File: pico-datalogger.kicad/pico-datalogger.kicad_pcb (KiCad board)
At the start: 2 copper layers, 80 x 90 mm, 28 parts, among them J1 JST-PH2 VCC, J10 Conn_Inky_SW, J2 Conn_I2C_Internal, J3 RFM9x_Lora_Breakout, J4 Alt-VCC, J5 Conn_I2S, J6 Conn_Inky_SPI, J7 Micro_SD_TF_PUSH, J8 Conn_ADC, J9 Conn_UART, SW1 SW_Push_SLIM, SW2 SW_Reset, U1 SN74HC74N, U2 PCF8523T, U3 Pico, Y1 Crystal

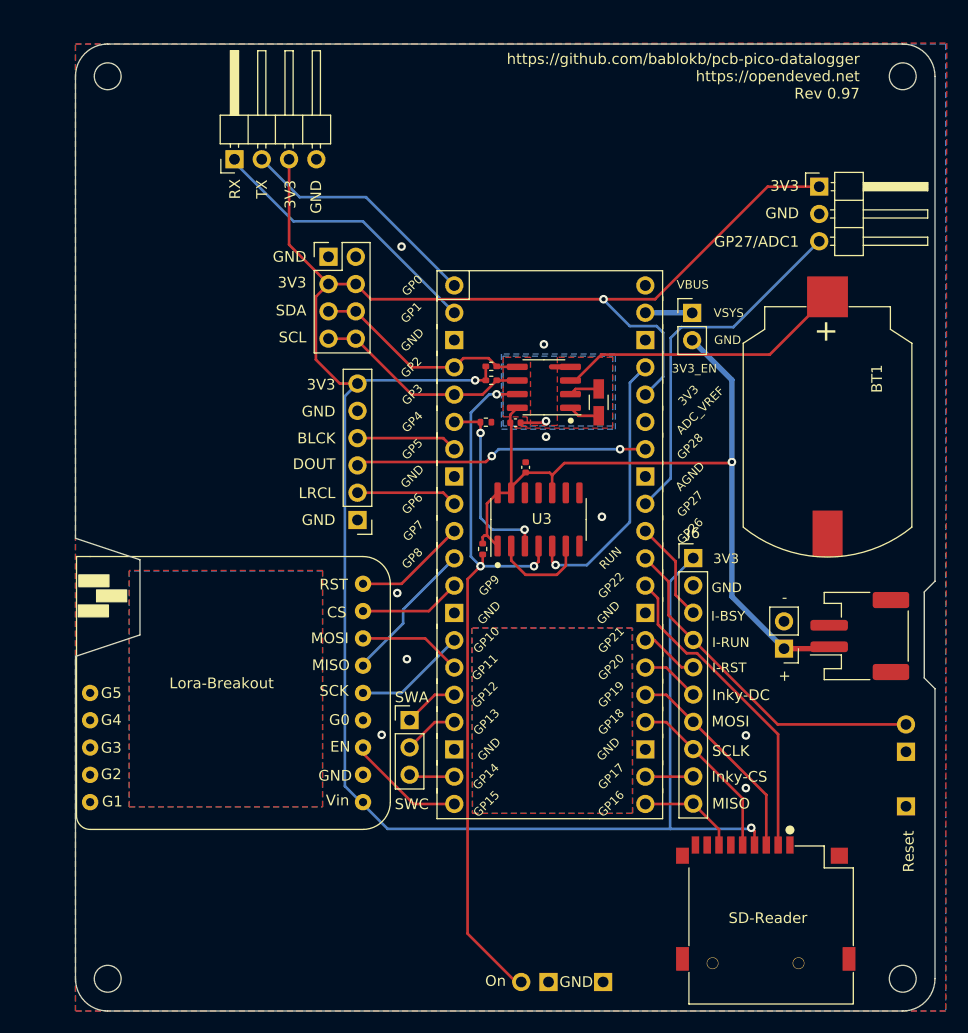
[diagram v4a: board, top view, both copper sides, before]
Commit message: added I2C/BG connectors
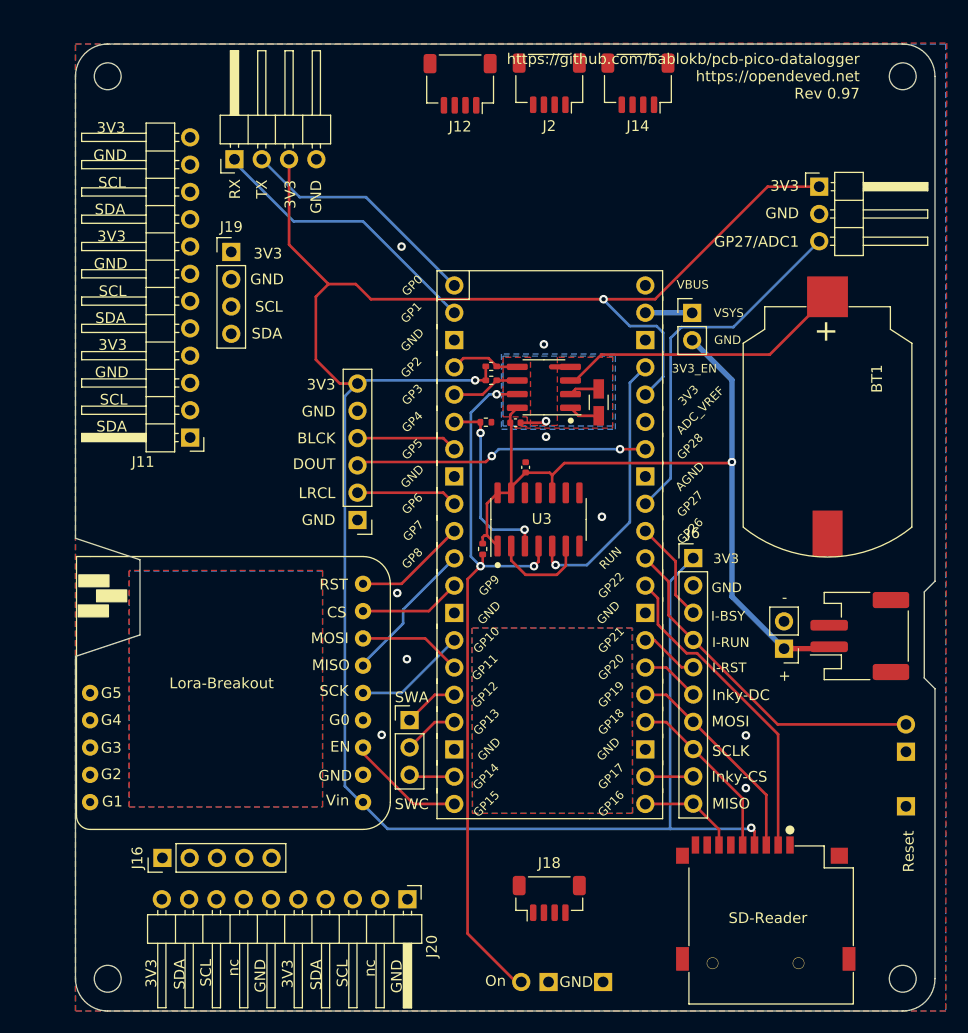
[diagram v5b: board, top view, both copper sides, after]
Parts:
- added J11: I2C_1, Connector_PinHeader_2.54mm:PinHeader_1x12_P2.54mm_Horizontal, F.Cu at (110.7, 86.6)
- added J12: I2C_7, Connector_JST:JST_SH_SM04B-SRSS-TB_1x04-1MP_P1.00mm_Horizontal, F.Cu at (135.8, 53.7)
- added J14: I2C_6, Connector_JST:JST_SH_SM04B-SRSS-TB_1x04-1MP_P1.00mm_Horizontal, F.Cu at (152.3, 53.6)
- added J16: BG_2, Connector_PinHeader_2.54mm:PinHeader_1x05_P2.54mm_Vertical, F.Cu at (108.1, 125.8)
- added J18: I2C_5, Connector_JST:JST_SH_BM04B-SRSS-TB_1x04-1MP_P1.00mm_Vertical, F.Cu at (144.1, 129.5)
- added J19: I2C_4, Connector_PinHeader_2.54mm:PinHeader_1x04_P2.54mm_Vertical, F.Cu at (114.5, 69.3)
- added J20: BG_3, Connector_PinHeader_2.54mm:PinHeader_1x10_P2.54mm_Horizontal, F.Cu at (130.9, 129.6)
- J2: value Conn_I2C_Internal -> I2C_8; footprint Connector_PinHeader_2.54mm:PinHeader_2x04_P2.54mm_Vertical -> Connector_JST:JST_SH_SM04B-SRSS-TB_1x04-1MP_P1.00mm_Horizontal
- moved J2 26.1 mm to (144.1, 53.6), turned to 180 degrees
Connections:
- J2 pad 1: GND -> +3V3
- J2 pad 3: +3V3 -> /SCL
- J2 pad 4: +3V3 -> /SDA
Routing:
- net /SDA: track 20.4 -> 6.55 mm
- net /SCL: track 20.3 -> 6.42 mm
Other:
- board text added: "nc"

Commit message: Rev 0.98: ready for production
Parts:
- added G***: LOGO, LOGO, B.Cu at (144.3, 66.4)
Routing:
- net /SCL: track 6.42 -> 204.3 mm, vias 0 -> 1
- net /SDA: track 6.55 -> 202.3 mm, vias 0 -> 2
- net +3V3: track 208.0 -> 299.9 mm, vias 3 -> 6
- net GND: vias 10 -> 13
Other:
- board text added: "BATT"
- board text added: "CR2032"
- board text added: "I2C"
- board text added: "I2C QT/Qwiic"
- board text added: "I2S"
- board text added: "MISO1"
- board text added: "MOSI1"
- board text added: "SCLK1"
- board text added: "UART"
- board text added: "https://github.com/bablokb/pcb-pico-datalogger https://opendeved.net/ilce Rev 0.98"
- board text removed: "MISO"
- board text removed: "MOSI"
- board text removed: "SCLK"
- board text removed: "https://github.com/bablokb/pcb-pico-datalogger https://opendeved.net Rev 0.97"

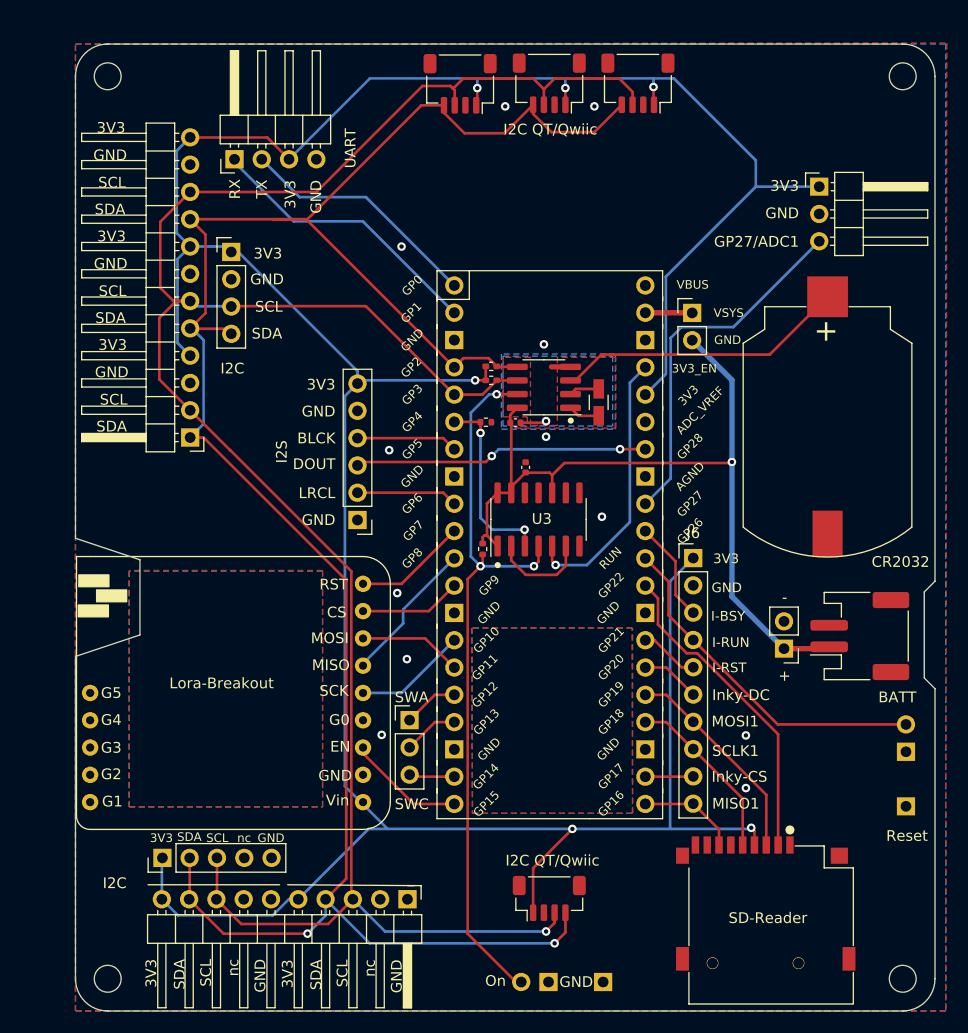
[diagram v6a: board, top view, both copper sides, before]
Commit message: Rev 1.00: fix Stemma/Qt connectors
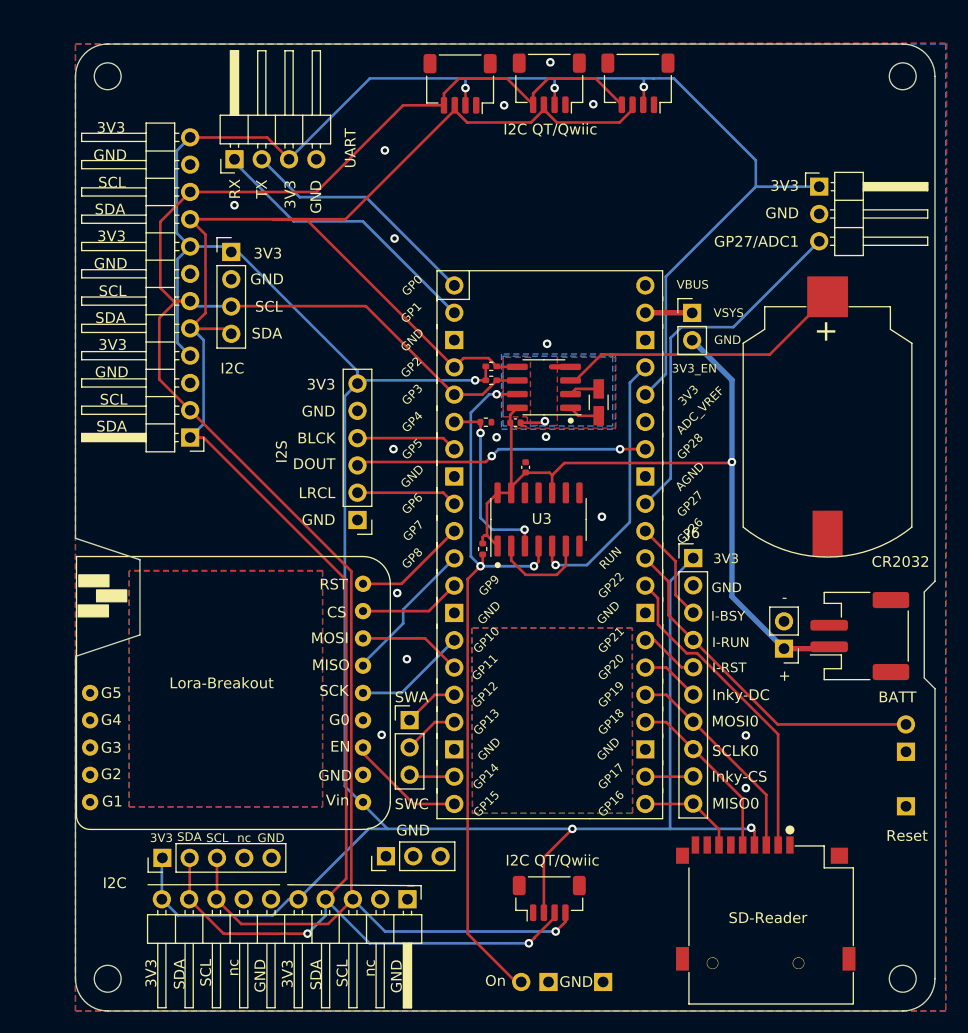
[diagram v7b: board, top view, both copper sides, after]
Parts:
- added J21: Conn_GND, Connector_PinHeader_2.54mm:PinHeader_1x03_P2.54mm_Vertical, F.Cu at (128.9, 125.6)
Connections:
- J12 pad 1: +3V3 -> GND
- J12 pad 2: GND -> +3V3
- J12 pad 3: /SCL -> /SDA
- J12 pad 4: /SDA -> /SCL
- J14 pad 1: +3V3 -> GND
- J14 pad 2: GND -> +3V3
- J14 pad 3: /SCL -> /SDA
- J14 pad 4: /SDA -> /SCL
- J18 pad 1: +3V3 -> GND
- J18 pad 2: GND -> +3V3
- J18 pad 3: /SCL -> /SDA
- J18 pad 4: /SDA -> /SCL
- J2 pad 1: +3V3 -> GND
- J2 pad 2: GND -> +3V3
- J2 pad 3: /SCL -> /SDA
- J2 pad 4: /SDA -> /SCL
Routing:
- net /SDA: track 202.3 -> 199.4 mm
- net /SCL: track 204.3 -> 202.7 mm
- net +3V3: track 299.9 -> 299.2 mm
- net GND: track 4.27 -> 4.17 mm, vias 13 -> 17
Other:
- board text added: "MISO0"
- board text added: "MOSI0"
- board text added: "SCLK0"
- board text added: "https://github.com/bablokb/pcb-pico-datalogger https://opendeved.net/ilce Rev 1.00"
- board text removed: "MISO1"
- board text removed: "MOSI1"
- board text removed: "SCLK1"
- board text removed: "https://github.com/bablokb/pcb-pico-datalogger https://opendeved.net/ilce Rev 0.98"
